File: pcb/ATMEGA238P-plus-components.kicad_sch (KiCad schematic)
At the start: 70 parts, among them J15 ICSP, J16 USB_B_Micro, J17 Conn_Coaxial, SW3 RST, U3 ATMEGA328P-AU, U4 CH340G, U5 LM358DR, U6 74HC245, U7 nRF24L01P, U9 74AHC1G125, Y3 16MHz, Y4 12MHz, Y5 16MHz

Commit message: pcb: source the tact switches as SHOU HAN TS24CA (C393942)
Give SW1 (STM32 reset), SW2 (user button), and SW3 (ATmega reset) a real
orderable part: footprint, LCSC/MPN fields, and datasheet, so they stop
blocking BOM/footprint coverage. One part number covers all three buttons;
side actuation keeps them reachable from the board edge. SW4 is deliberately
untouched — it is the master power switch and needs a latching, adequately
rated part, tracked in DESIGN_REVIEW and the new parts log.
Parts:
- SW3: value RST -> TS24CA_C393942; footprint (none) -> easyeda:SW-SMD_2P-TS24CA; LCSC (none) -> C393942; Manufacturer (none) -> SHOU HAN; Part (none) -> TS24CA
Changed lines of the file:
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@@
 			)
 		)
-		(property "Value" "RST"
+		(property "Value" "TS24CA_C393942"
 			(at 33.02 40.6399 90)
 			(show_name no)
@@
 			)
 		)
-		(property "Footprint" ""
+		(property "Footprint" "easyeda:SW-SMD_2P-TS24CA"
 			(at 34.29 39.37 0)
 			(hide yes)
@@
 			)
 		)
-		(property "Datasheet" ""
+		(property "Datasheet" "https://www.lcsc.com/datasheet/lcsc_datasheet_2404241539_SHOU-HAN-TS24CA_C393942.pdf"
 			(at 34.29 39.37 0)
 			(hide yes)
@@
 			)
 		)
-		(property "Description" "Push button switch, generic, two pins"
+		(property "Description" "-20℃~+70℃ 1.6N 1.9mm 12V 20,000 cycles 3.5mm 4.7mm 50mA Black No Rectangular Button SMD(SMT) Tab SPST Surface Mount, Right Angle Without Bracket SMD,4.6x1.8mm Tactile Switches ROHS"
 			(at 29.21 39.37 0)
 			(hide yes)
@@
 			)
 		)
+    (property "LCSC" "C393942" (at 29.21 39.37 0)
+      (effects (font (size 1.27 1.27)) (hide yes))
+    )
+    (property "Part" "TS24CA" (at 29.21 39.37 0)
+      (effects (font (size 1.27 1.27)) (hide yes))
+    )
+    (property "Manufacturer" "SHOU HAN" (at 29.21 39.37 0)
+      (effects (font (size 1.27 1.27)) (hide yes))
+    )
 		(pin "2"
 		)

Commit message: footprint assignments
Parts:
- C20, C21, C22, C23, C24, C25, C26, C27, C28, C29, C30, C31, C32, C33, C34, C35, C36, C37, C38, C39, C40, C41, C42, C43, C44, C45, C46, C47: footprint (none) -> Capacitor_SMD:C_0402_1005Metric
- D10: footprint (none) -> Diode_SMD:D_SOD-123
- D11, D12, D13, D15, D16, D18: footprint (none) -> LED_SMD:LED_0603_1608Metric
- J15: footprint (none) -> Connector_PinHeader_2.54mm:PinHeader_2x03_P2.54mm_Vertical
- J16: footprint (none) -> easyeda:MICRO-USB-SMD_5P-P0.65-H-F_MICRO5.9MMUSB
- J17: footprint (none) -> easyeda:SMA_142-0701-201
- L2, L3, L4: footprint (none) -> Inductor_SMD:L_0402_1005Metric
- R21, R22, R24, R25, R26, R27, R30, R33, R35, R36, R37, R38: footprint (none) -> Resistor_SMD:R_0402_1005Metric
- R23, R28, R29, R31, R32, R34: footprint (none) -> Resistor_SMD:R_0603_1608Metric
- U6: footprint (none) -> Package_SO:SOIC-20W_7.5x12.8mm_P1.27mm
- U8: value (none) -> MICROSD_C164170
- U9: footprint (none) -> Package_TO_SOT_SMD:SOT-353_SC-70-5
- Y3, Y4, Y5: footprint (none) -> Crystal:Crystal_SMD_SeikoEpson_TSX3225-4Pin_3.2x2.5mm

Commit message: erc: first clean native run, plus full footprint assignment
Fix the CH340G VCC/V3 cross-wiring (the chip was unpowered and its
internal 3.3 V node sat on the 5 V rail), add PWR_FLAGs to the
passive-fed rails and GND, no-connect SW4's unused throw, and retype
the USB shell grounds to passive - ERC now reports 0/0 on both sheets.
Assign footprints to every remaining component and import all 158 into
the board so layout can start. Two known netlist gaps recorded in
DESIGN_REVIEW: the USB shield pads (symbol SH vs footprint 6) and the
nRF24 exposed pad are floating; MPN coverage is still four parts.
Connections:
- net V3: now also U4.4 (V3); no longer U4.16 (VCC)
- net Vdrive: now also U4.16 (VCC); no longer U4.4 (V3)
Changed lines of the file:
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@@
 	)
 	(junction
+		(at 66.04 223.52)
+		(diameter 0)
+		(color 0 0 0 0)
+	)
+	(junction
 		(at 298.45 242.57)
 		(diameter 0)
@@
 	(wire
 		(pts
+			(xy 66.04 222.25) (xy 66.04 223.52)
+		)
+		(stroke
+			(width 0)
+			(type default)
+		)
+	)
+	(wire
+		(pts
 			(xy 73.66 273.05) (xy 95.25 273.05)
 		)
@@
 	(wire
 		(pts
+			(xy 66.04 223.52) (xy 66.04 224.79)
+		)
+		(stroke
+			(width 0)
+			(type default)
+		)
+	)
+	(wire
+		(pts
 			(xy 29.21 205.74) (xy 22.86 205.74)
 		)
@@
 	(wire
 		(pts
+			(xy 39.37 256.54) (xy 39.37 259.08)
+		)
+		(stroke
+			(width 0)
+			(type default)
+		)
+	)
+	(wire
+		(pts
 			(xy 68.58 264.16) (xy 67.31 264.16)
 		)
@@
 	(wire
 		(pts
-			(xy 66.04 246.38) (xy 46.99 246.38)
-		)
-		(stroke
-			(width 0)
-			(type default)
-		)
-	)
-	(wire
-		(pts
 			(xy 173.99 36.83) (xy 168.91 36.83)
 		)
@@
 	(wire
 		(pts
+			(xy 46.99 246.38) (xy 66.04 246.38)
+		)
+		(stroke
+			(width 0)
+			(type default)
+		)
+	)
+	(wire
+		(pts
 			(xy 389.89 143.51) (xy 394.97 143.51)
 		)
@@
 		)
 	)
-	(global_label "V3"
-		(shape input)
-		(at 102.87 228.6 180)
-		(fields_autoplaced yes)
-		(effects
-			(font
-				(size 1.27 1.27)
-			)
-			(justify right)
-		)
-		(property "Intersheetrefs" "${INTERSHEET_REFS}"
-			(at 97.5867 228.6 0)
-			(hide yes)
-			(show_name no)
-			(do_not_autoplace no)
-			(effects
-				(font
-					(size 1.27 1.27)
-				)
-				(justify right)
-			)
-		)
-	)
 	(global_label "CS_nRF_74HC245"
 		(shape input)
@@
 		)
 	)
+	(global_label "V3"
+		(shape input)
+		(at 105.41 228.6 90)
+		(fields_autoplaced yes)
+		(effects
+			(font
+				(size 1.27 1.27)
+			)
+			(justify left)
+		)
+		(property "Intersheetrefs" "${INTERSHEET_REFS}"
+			(at 105.41 223.3167 90)
+			(hide yes)
+			(show_name no)
+			(do_not_autoplace no)
+			(effects
+				(font
+					(size 1.27 1.27)
+				)
+				(justify left)
+			)
+		)
+	)
 	(global_label "SCK_ATM328P"
 		(shape input)
@@
 	(symbol
 		(lib_id "power:Vdrive")
-		(at 66.04 224.79 0)
+		(at 66.04 222.25 0)
 		(unit 1)
 		(body_style 1)
@@
 		(dnp no)
 		(property "Reference" "#PWR083"
-			(at 66.04 228.6 0)
+			(at 66.04 226.06 0)
 			(hide yes)
 			(show_name no)
@@
 		)
 		(property "Value" "Vdrive"
-			(at 66.04 220.726 0)
+			(at 66.04 218.186 0)
 			(show_name no)
 			(do_not_autoplace no)
@@
 		)
 		(property "Footprint" ""
-			(at 66.04 224.79 0)
+			(at 66.04 222.25 0)
 			(hide yes)
 			(show_name no)
@@
 		)
 		(property "Datasheet" ""
-			(at 66.04 224.79 0)
+			(at 66.04 222.25 0)
 			(hide yes)
 			(show_name no)
@@
 		)
 		(property "Description" "Power symbol creates a global label with name \"Vdrive\""
-			(at 66.04 224.79 0)
+			(at 66.04 222.25 0)
 			(hide yes)
 			(show_name no)
@@
 	(symbol
 		(lib_id "PCM_SparkFun-PowerSymbol:GND")
-		(at 39.37 256.54 0)
+		(at 39.37 259.08 0)
 		(unit 1)
 		(body_style 1)
@@
 		(fields_autoplaced yes)
 		(property "Reference" "#PWR079"
-			(at 39.37 262.89 0)
+			(at 39.37 265.43 0)
 			(hide yes)
 			(show_name no)
@@
 		)
 		(property "Value" "GND"
-			(at 39.37 260.35 0)
+			(at 39.37 262.89 0)
 			(show_name no)
 			(do_not_autoplace yes)
@@
 		)
 		(property "Footprint" ""
-			(at 39.37 256.54 0)
+			(at 39.37 259.08 0)
 			(hide yes)
 			(show_name no)
@@
 		)
 		(property "Datasheet" ""
-			(at 39.37 256.54 0)
+			(at 39.37 259.08 0)
 			(hide yes)
 			(show_name no)
@@
 		)
 		(property "Description" "Power symbol creates a global label with name \"GND\" , ground"
-			(at 39.37 265.43 0)
+			(at 39.37 267.97 0)
 			(hide yes)
 			(show_name no)
@@
 			)
 		)
-		(property "Description" "-20℃~+70℃ 1.6N 1.9mm 12V 20,000 cycles 3.5mm 4.7mm 50mA Black No Rectangular Button SMD(SMT) Tab SPST Surface Mount, Right Angle Without Bracket SMD,4.6x1.8mm Tactile Switches ROHS"
+		(property "Description" "Push button switch, generic, two pins"
 			(at 29.21 39.37 0)
 			(hide yes)
@@
 	)
 	(symbol
+		(lib_id "power:PWR_FLAG")
+		(at 66.04 223.52 90)
+		(unit 1)
+		(body_style 1)
+		(exclude_from_sim no)
+		(in_bom yes)
+		(on_board yes)
+		(in_pos_files yes)
+		(dnp no)
+		(fields_autoplaced yes)
+		(property "Reference" "#FLG05"
+			(at 64.135 223.52 0)
+			(hide yes)
+			(show_name no)
+			(do_not_autoplace no)
+			(effects
+				(font
+					(size 1.27 1.27)
+				)
+			)
+		)
+		(property "Value" "PWR_FLAG"
+			(at 62.23 223.5199 90)
+			(show_name no)
+			(do_not_autoplace no)
+			(effects
+				(font
+					(size 1.27 1.27)
+				)
+				(justify left)
+			)
+		)
+		(property "Footprint" ""
+			(at 66.04 223.52 0)
+			(hide yes)
+			(show_name no)
+			(do_not_autoplace no)
+			(effects
+				(font
+					(size 1.27 1.27)
+				)
+			)
+		)
+		(property "Datasheet" ""
+			(at 66.04 223.52 0)
+			(hide yes)
+			(show_name no)
+			(do_not_autoplace no)
+			(effects
+				(font
+					(size 1.27 1.27)
+				)
+			)
+		)
+		(property "Description" "Special symbol for telling ERC where power comes from"
+			(at 66.04 223.52 0)
+			(hide yes)
+			(show_name no)
+			(do_not_autoplace no)
+			(effects
+				(font
+					(size 1.27 1.27)
+				)
+			)
+		)
+		(pin "1"
+		)
+		(instances
+			(project "drone-flight-controller"
+				(path "/2753c1d5-c5b3-42f6-8923-cca974813b6b/3ba11137-7aba-429f-b0d2-26d56a1546d6"
+					(reference "#FLG05")
+					(unit 1)
+				)
+			)
+		)
+	)
+	(symbol
 		(lib_id "Device:C_Small")
 		(at 289.56 175.26 0)
@@
 	(symbol
 		(lib_id "power:Vdrive")
-		(at 105.41 228.6 0)
+		(at 102.87 228.6 90)
 		(unit 1)
 		(body_style 1)
@@
 		(in_pos_files yes)
 		(dnp no)
-		(property "Reference" "#PWR078"
-			(at 105.41 232.41 0)
+		(property "Reference" "#PWR0141"
+			(at 106.68 228.6 0)
 			(hide yes)
 			(show_name no)
@@
 		)
 		(property "Value" "Vdrive"
-			(at 105.41 224.536 0)
+			(at 96.774 228.6 90)
 			(show_name no)
 			(do_not_autoplace no)
@@
 		)
 		(property "Footprint" ""
-			(at 105.41 228.6 0)
+			(at 102.87 228.6 0)
 			(hide yes)
 			(show_name no)
@@
 		)
 		(property "Datasheet" ""
-			(at 105.41 228.6 0)
+			(at 102.87 228.6 0)
 			(hide yes)
 			(show_name no)
@@
 		)
 		(property "Description" "Power symbol creates a global label with name \"Vdrive\""
-			(at 105.41 228.6 0)
+			(at 102.87 228.6 0)
 			(hide yes)
 			(show_name no)
@@
 			(project "drone-flight-controller"
 				(path "/2753c1d5-c5b3-42f6-8923-cca974813b6b/3ba11137-7aba-429f-b0d2-26d56a1546d6"
-					(reference "#PWR078")
+					(reference "#PWR0141")
 					(unit 1)
 				)

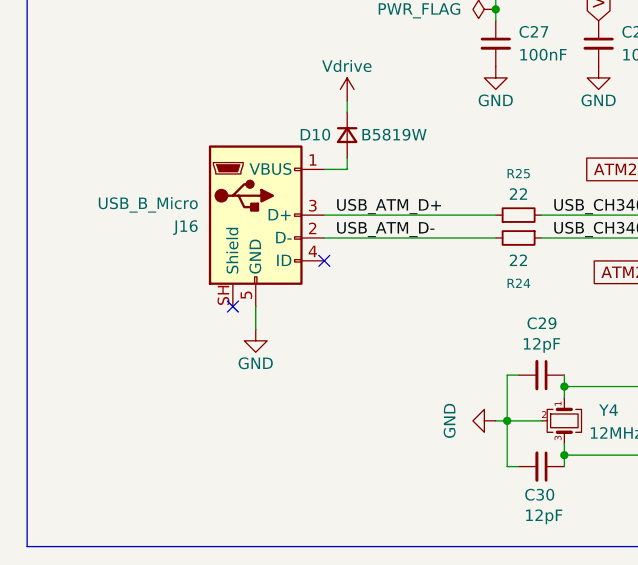
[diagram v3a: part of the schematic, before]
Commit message: pcb: ground the USB shields; leave the nRF24 EP per datasheet
The Update-PCB import exposed that J3/J16's shield pin was numbered SH
while the footprint's shell pads are numbered 6, and the pin was not
wired to anything - both connector shells would have floated. Renumber
the pin to 6 (KiCad's own USB symbol convention) and tie it to GND.
U7's exposed pad is deliberately left unconnected: the nRF24L01+
Product Specification v1.0 (p. 65) recommends keeping the die attach
pad unconnected, so the pad-21 import warning is expected.
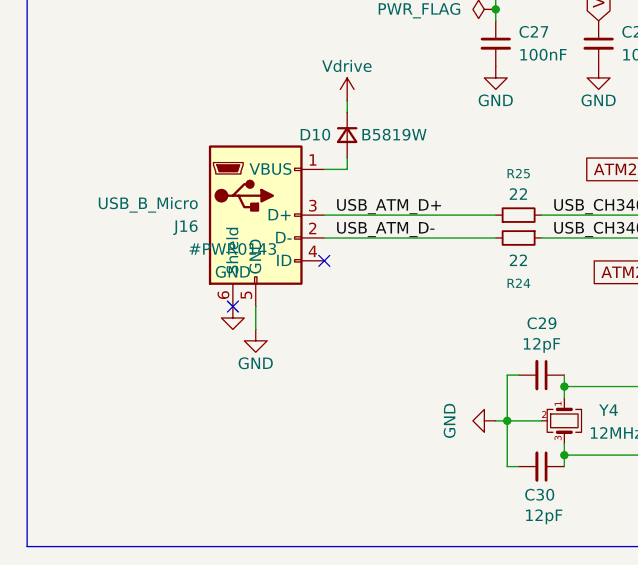
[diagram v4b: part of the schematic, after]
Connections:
- net GND: now also J16.6 (Shield)
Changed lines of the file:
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@@
 		(pin "1"
 		)
-		(pin "SH"
+		(pin "6"
 		)
 		(pin "4"
@@
 		)
 	)
+  (symbol (lib_id "power:GND") (at 36.83 256.54 0) (unit 1)
+    (in_bom yes) (on_board yes) (dnp no)
+    (property "Reference" "#PWR0143" (at 36.83 250.19 0.0)
+      (effects
+					(font
+						(size 1.27 1.27)
+					)
+				)
+    )
+    (property "Value" "GND" (at 36.83 252.73 0.0)
+      (effects
+					(font
+						(size 1.27 1.27)
+					)
+				)
+    )
+    (property "Footprint" "" (at 36.83 256.54 0)
+      (effects (font (size 1.27 1.27)) (hide yes))
+    )
+    (property "Datasheet" "~" (at 36.83 256.54 0)
+      (effects (font (size 1.27 1.27)) (hide yes))
+    )
+    (instances
+      (project "project"
+        (path "/"
+          (reference "#PWR0143")
+          (unit 1)
+        )
+      )
+    )
+  )
 )
